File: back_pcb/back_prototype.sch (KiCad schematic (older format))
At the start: 84 parts, among them P1 EXPANSION_LEFT, P2 EXPANSION_BOTTOM, P3 EXPANSION_TOP, P4 USB_A, P5 AUDIO_CONN, P6 ATMEGA_HEADER, P7 EXPANSION_BOTTOM2, P8 CONN_01X02, Q1 IRLML6401, Q2 BSS138, Q3 BSS138, Q4 IRLML6401, U1 PI ZERO, U2 SIM800_BREAKOUT, U3 MCP23017, U4 TP4056_BREAKOUT, U5 RTC, U6 DC_DC_BREAKOUT, Y1 32.768Hz

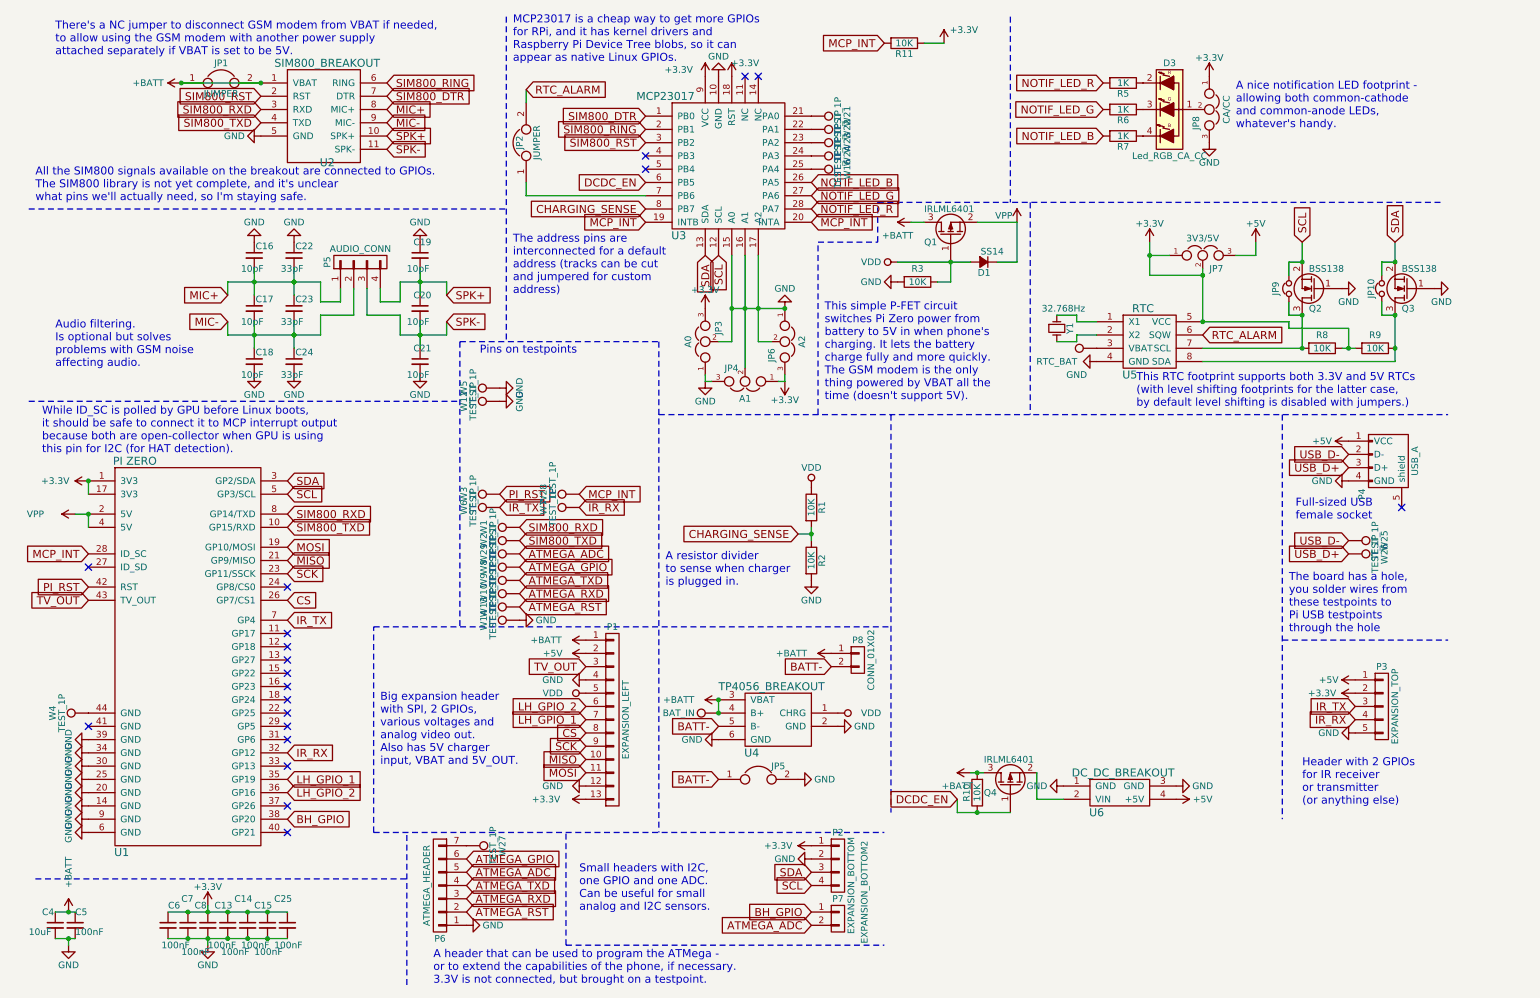
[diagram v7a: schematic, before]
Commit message: Back board sch - pin swapping
Pins rearranged for gamma revision
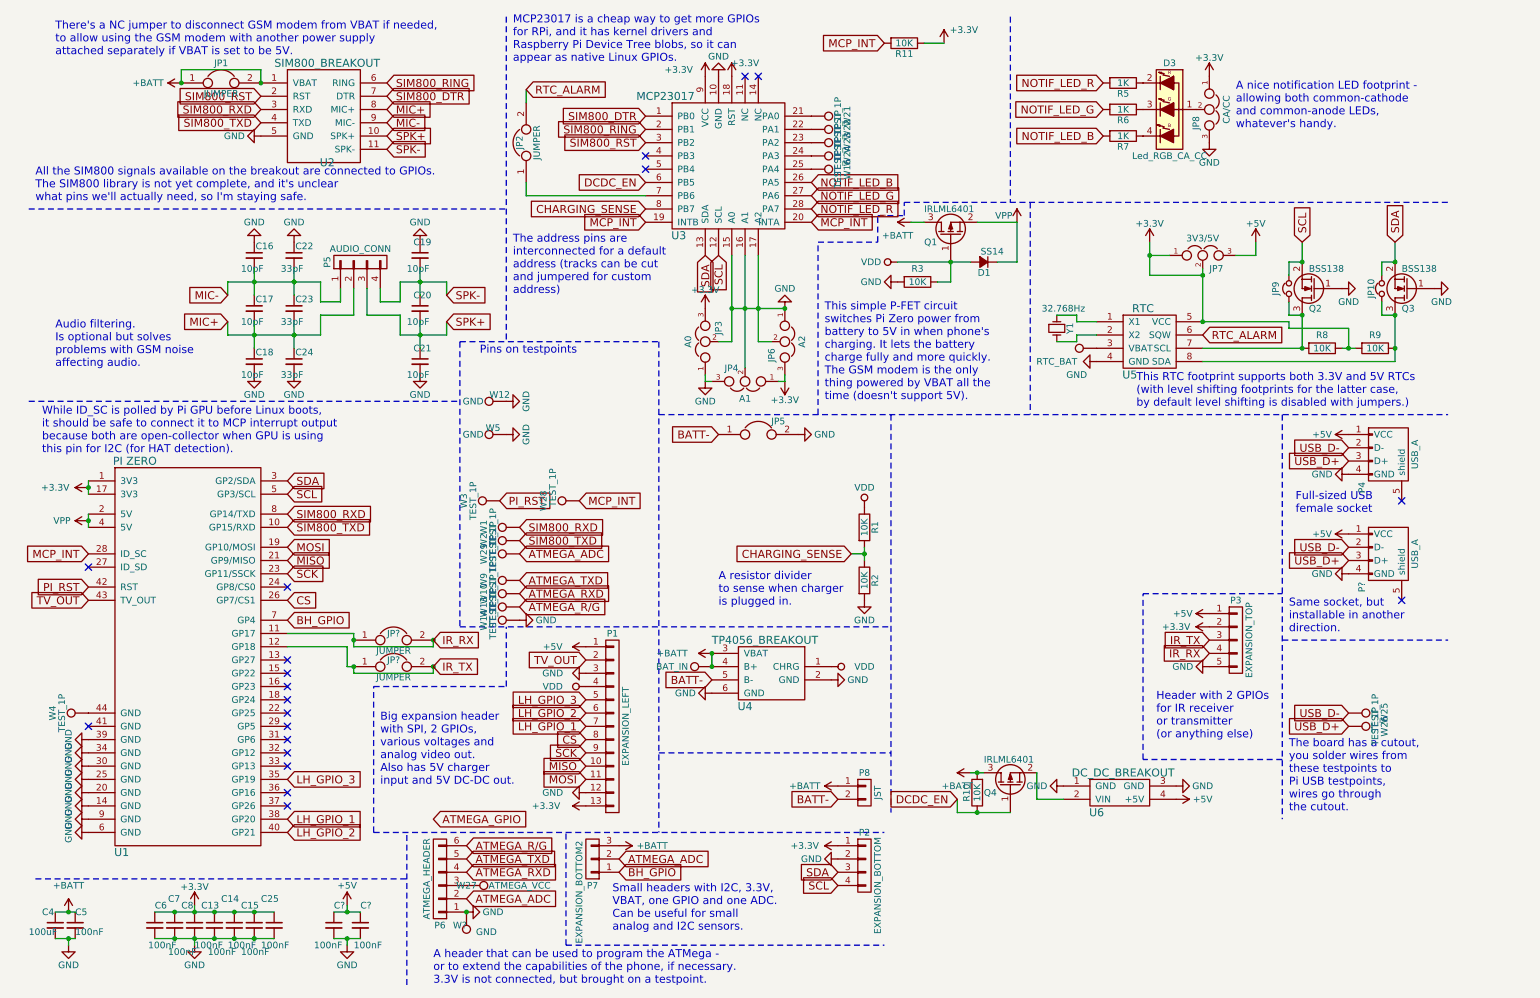
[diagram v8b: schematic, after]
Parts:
- removed P6: ATMEGA_HEADER, Pin_Headers:Pin_Header_Straight_1x07_Pitch2.54mm, symbol CONN_01X07
- removed P7: EXPANSION_BOTTOM2, Pin_Headers:Pin_Header_Angled_1x02_Pitch2.54mm, symbol CONN_01X02
- removed W6, W7, W8: TEST_1P, Measurement_Points:Measurement_Point_Square-SMD-Pad_Small, symbol TEST_1P
- added C? (x2): 100nF, Capacitors_SMD:C_0805, symbol C_Small
- added JP? (x2): JUMPER, Connect:GS2, symbol JUMPER
- added P6: ATMEGA_HEADER, symbol CONN_01X06
- added P7: EXPANSION_BOTTOM2, symbol CONN_01X03
- added P?: USB_A, Connect:USB_A, symbol USB_A
- added W?: GND, Measurement_Points:Measurement_Point_Square-SMD-Pad_Small, symbol TEST_1P
- C4: value 10uF -> 100uF
- P8: value CONN_01X02 -> JST
- W12, W5: value TEST_1P -> GND
- W27: value TEST_1P -> ATMEGA_VCC
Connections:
- net +5V: now also P1.1 (P1), C?.1, C?.1, P?.1 (VCC); no longer P1.2 (P2)
- net +BATT: now also P7.3 (P3); no longer P1.1 (P1)
- net ATMEGA_ADC: now also P6.2 (P2), P7.2 (P2)
- net ATMEGA_RXD: now also P6.4 (P4)
- net ATMEGA_TXD: now also P6.5 (P5)
- net BH_GPIO: now also U1.7 (GP4), P7.1 (P1); no longer U1.38 (GP20)
- net GND: now also P1.3 (P3), C?.2, C?.2, P6.1 (P1), P?.4 (GND), W?.1; no longer P1.4 (P4)
- net IR_RX: now also U1.11 (GP17), JP?.1, JP?.2; no longer U1.32 (GP12)
- net IR_TX: now also U1.12 (GP18), JP?.1, JP?.2; no longer U1.7 (GP4)
- net LH_GPIO_1: now also U1.38 (GP20); no longer U1.35 (GP19)
- net LH_GPIO_2: now also U1.40 (GP21); no longer U1.36 (GP16)
- net MIC+: now also C17.2, C18.1, C23.2, C24.1, P5.2 (P2); no longer C16.2, C17.1, C22.2, C23.1, P5.1 (P1)
- net MIC-: now also C16.2, C17.1, C22.2, C23.1, P5.1 (P1); no longer C17.2, C18.1, C23.2, C24.1, P5.2 (P2)
- net SPK+: now also C20.2, C21.1, P5.3 (P3); no longer C19.2, C20.1, P5.4 (P4)
- net SPK-: now also C19.2, C20.1, P5.4 (P4); no longer C20.2, C21.1, P5.3 (P3)
- net TV_OUT: now also P1.2 (P2); no longer P1.3 (P3)
- net USB_D+: now also P?.3 (D+)
- net USB_D-: now also P?.2 (D-)
- net VDD: now also P1.4 (P4); no longer P1.5 (P5)
- net at W27.1: now also P6.3 (P3)
- net ATMEGA_RST renamed ATMEGA_R/G
- net ATMEGA_R/G: now also P6.6 (P6)
- new net LH_GPIO_3: P1.5 (P5), U1.35 (GP19)
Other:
- note added: "Big expansion header \nwith SPI, 2 GPIOs, \nvarious voltages and \nanalog video out.\nAlso has 5V charger \ninput and 5V DC-DC out."
- note added: "Same socket, but\ninstallable in another\ndirection."
- note added: "Small headers with I2C, 3.3V,\nVBAT, one GPIO and one ADC. \nCan be useful for small \nanalog and I2C sensors."
- note added: "The board has a cutout,\nyou solder wires from\nthese testpoints to\nPi USB testpoints,\nwires go through\nthe cutout."
- note added: "While ID_SC is polled by Pi GPU before Linux boots, \nit should be safe to connect it to MCP interrupt output \nbecause both are open-collector when GPU is using\nthis pin for I2C (for HAT detection)."
- note removed: "Big expansion header \nwith SPI, 2 GPIOs, \nvarious voltages and \nanalog video out.\nAlso has 5V charger \ninput, VBAT and 5V_OUT."
- note removed: "Small headers with I2C, \none GPIO and one ADC. \nCan be useful for small \nanalog and I2C sensors."
- note removed: "The board has a hole,\nyou solder wires from\nthese testpoints to\nPi USB testpoints\nthrough the hole"
- note removed: "While ID_SC is polled by GPU before Linux boots, \nit should be safe to connect it to MCP interrupt output \nbecause both are open-collector when GPU is using\nthis pin for I2C (for HAT detection)."
- moved on the sheet: C13, C14, C15, C25, C6, C7, C8, JP5, P1, P2, P3, P4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
